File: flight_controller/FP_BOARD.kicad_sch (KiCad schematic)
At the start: 4 parts

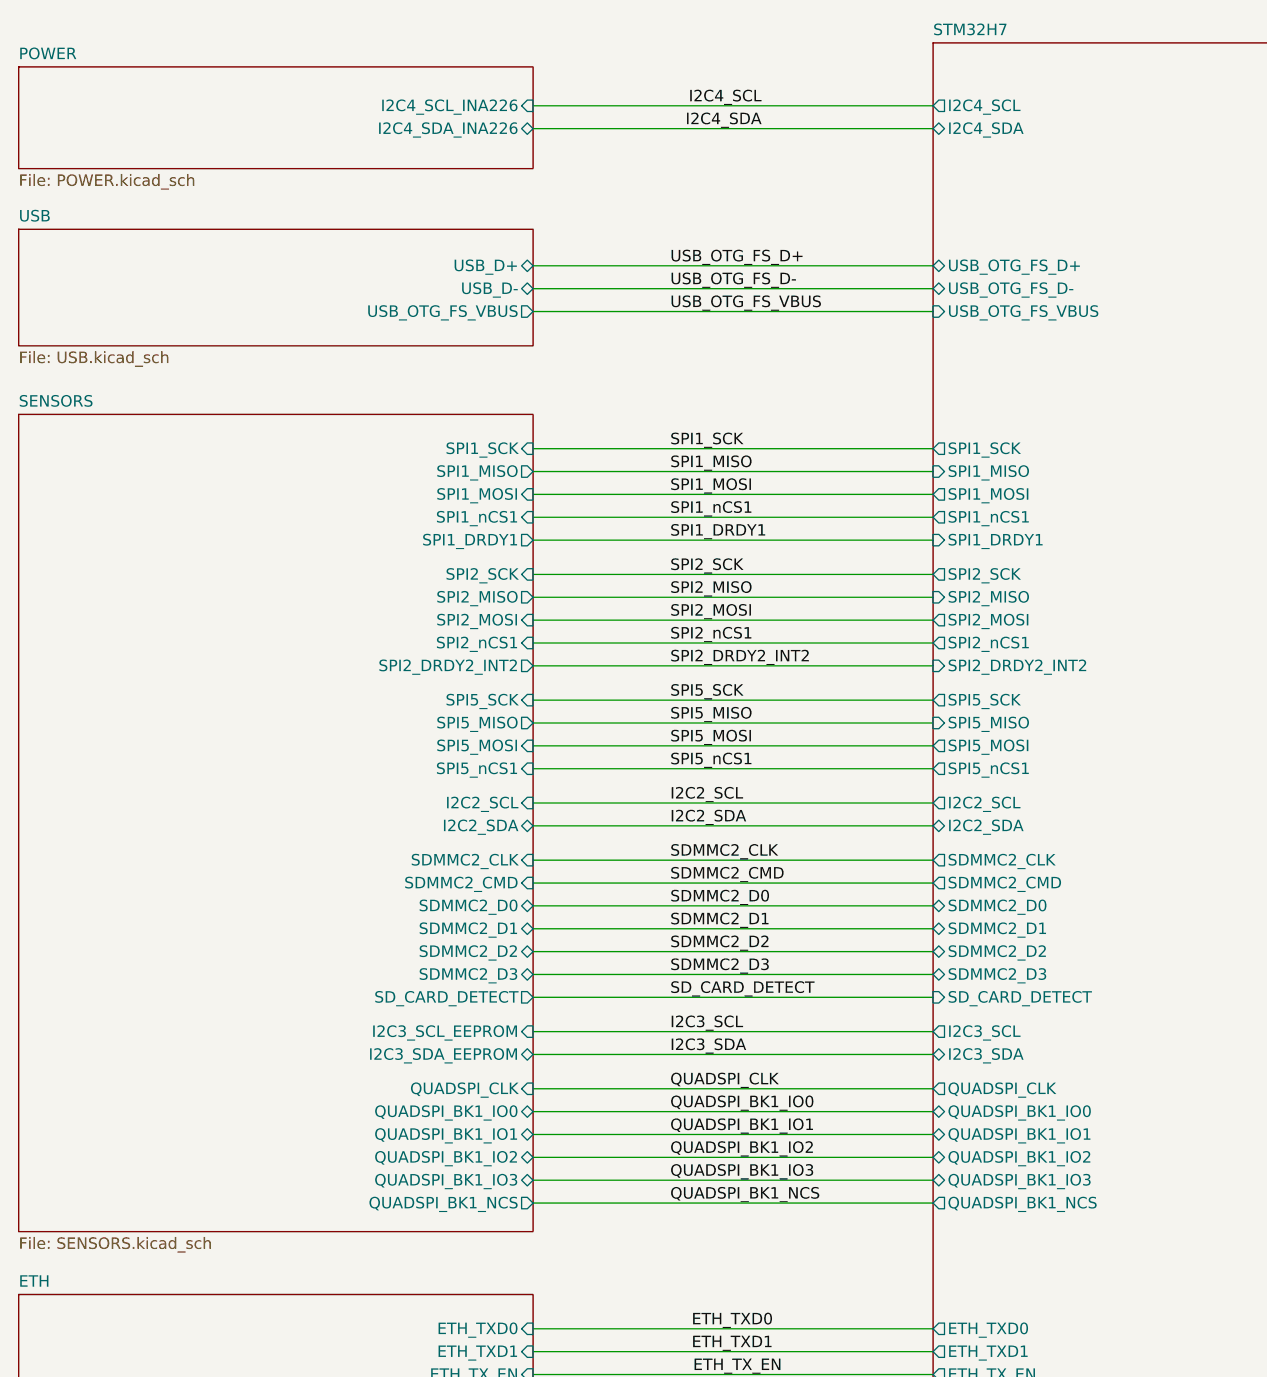
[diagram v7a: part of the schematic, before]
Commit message: Revert to state of commit 2458262 moved all to components to top
Reverts commits: d012532, 3d9c600, 58bc0ac
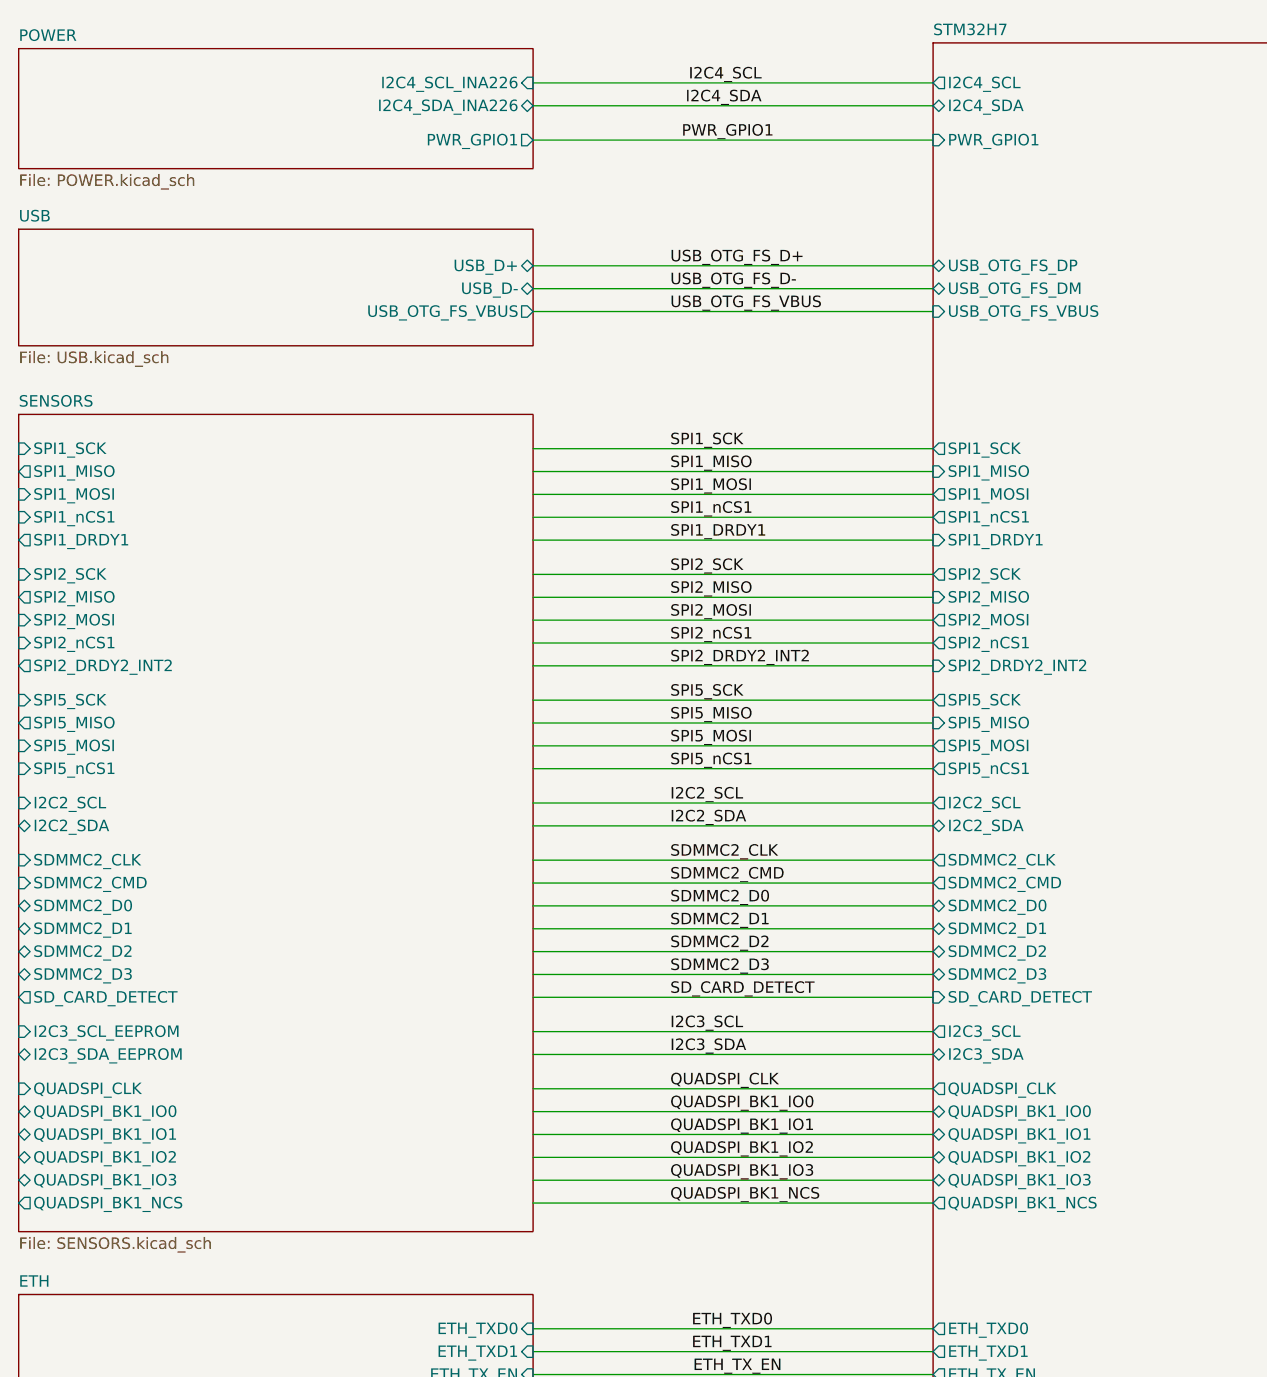
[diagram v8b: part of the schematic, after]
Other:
- sheet POWER ports: added PWR_GPIO1; removed none
- sheet STM32H7 ports: added PWR_GPIO1, USB_OTG_FS_DM, USB_OTG_FS_DP; removed USB_OTG_FS_D+, USB_OTG_FS_D-
